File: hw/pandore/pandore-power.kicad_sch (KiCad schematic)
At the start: 57 parts, among them J14 V12, J20 V5, J21 V3.3, J32 VSTBY, J6 VIN, Q5 MOSFET_EN-N, Q6 MOSFET_EN-N, U19 AP6335xQ, U20 AP6335xQ, U27 LDL212DR

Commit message: added monitor amp with volume knob continue routing all around
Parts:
- R129, R133: now not fitted
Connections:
- net PWRON: now also R129.2, R130.1, R133.2, R134.1, U19.2 (EN), U20.2 (EN)
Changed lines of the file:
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@@
 	)
 	(junction
+		(at 97.79 116.84)
+		(diameter 0)
+		(color 0 0 0 0)
+	)
+	(junction
 		(at 101.6 35.56)
 		(diameter 0)
@@
 	(wire
 		(pts
+			(xy 97.79 116.84) (xy 97.79 68.58)
+		)
+		(stroke
+			(width 0)
+			(type default)
+		)
+	)
+	(wire
+		(pts
 			(xy 92.71 35.56) (xy 92.71 38.1)
 		)
@@
 	(wire
 		(pts
-			(xy 33.02 116.84) (xy 48.26 116.84)
+			(xy 33.02 116.84) (xy 97.79 116.84)
 		)
 		(stroke
@@
 	(wire
 		(pts
+			(xy 97.79 68.58) (xy 123.19 68.58)
+		)
+		(stroke
+			(width 0)
+			(type default)
+		)
+	)
+	(wire
+		(pts
 			(xy 182.88 55.88) (xy 182.88 57.15)
 		)
@@
 	(wire
 		(pts
+			(xy 97.79 116.84) (xy 123.19 116.84)
+		)
+		(stroke
+			(width 0)
+			(type default)
+		)
+	)
+	(wire
+		(pts
 			(xy 101.6 55.88) (xy 101.6 104.14)
 		)
@@
 		(in_bom yes)
 		(on_board yes)
-		(dnp no)
+		(dnp yes)
 		(fields_autoplaced yes)
 		(property "Reference" "R129"
@@
 		(in_bom yes)
 		(on_board yes)
-		(dnp no)
+		(dnp yes)
 		(fields_autoplaced yes)
 		(property "Reference" "R133"

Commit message: last sprint almost done, most routing done
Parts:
- added Q16: MOSFET_EN-P, reekilib_dfn:DFN65P300X300X100-9, symbol reekilib_mfe:MOSFET_EN-P_8pin
- added R276, R277: ${Resistance}, ${Tolerance}, ${Power}, reekilib_res:RESC1005, symbol reekilib_res:res
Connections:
- net V12: now also Q16.1 (S), Q16.2 (S), Q16.3 (S), R276.2
- net VSS: now also R277.1
- net at J6.1 (TIP): now also Q16.5 (D), Q16.6 (D), Q16.7 (D), Q16.8 (D), Q16.9 (D)
- new net: Q16.4 (G), R276.1, R277.2

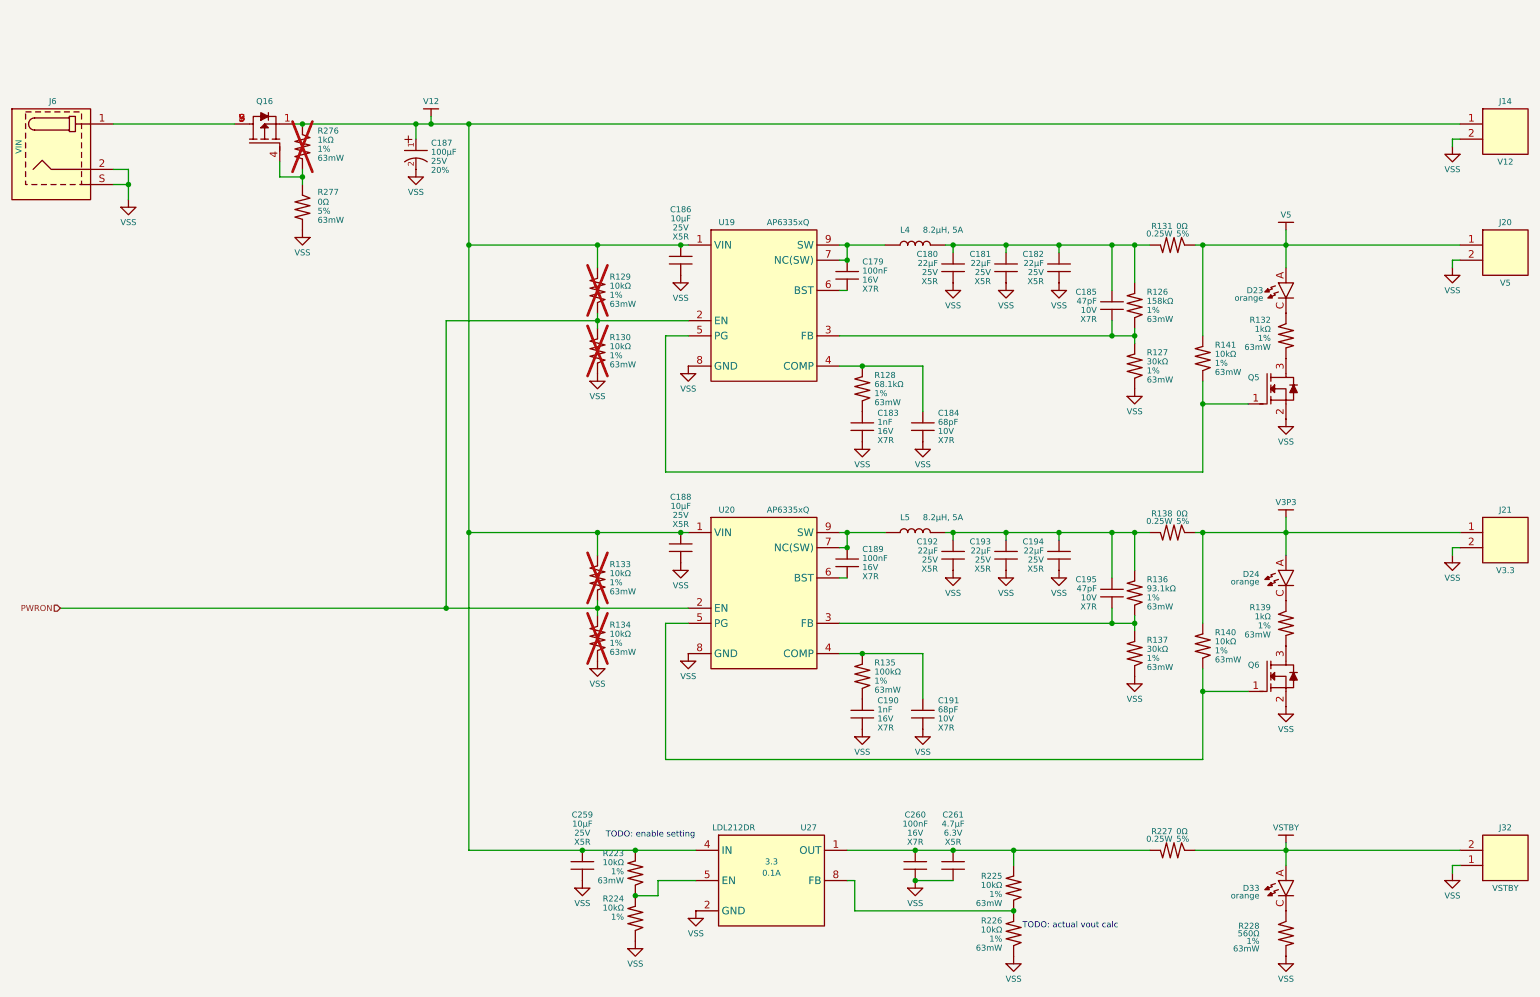
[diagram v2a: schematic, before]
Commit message: finished adding mpn,mfg to all parts, finished routing placement
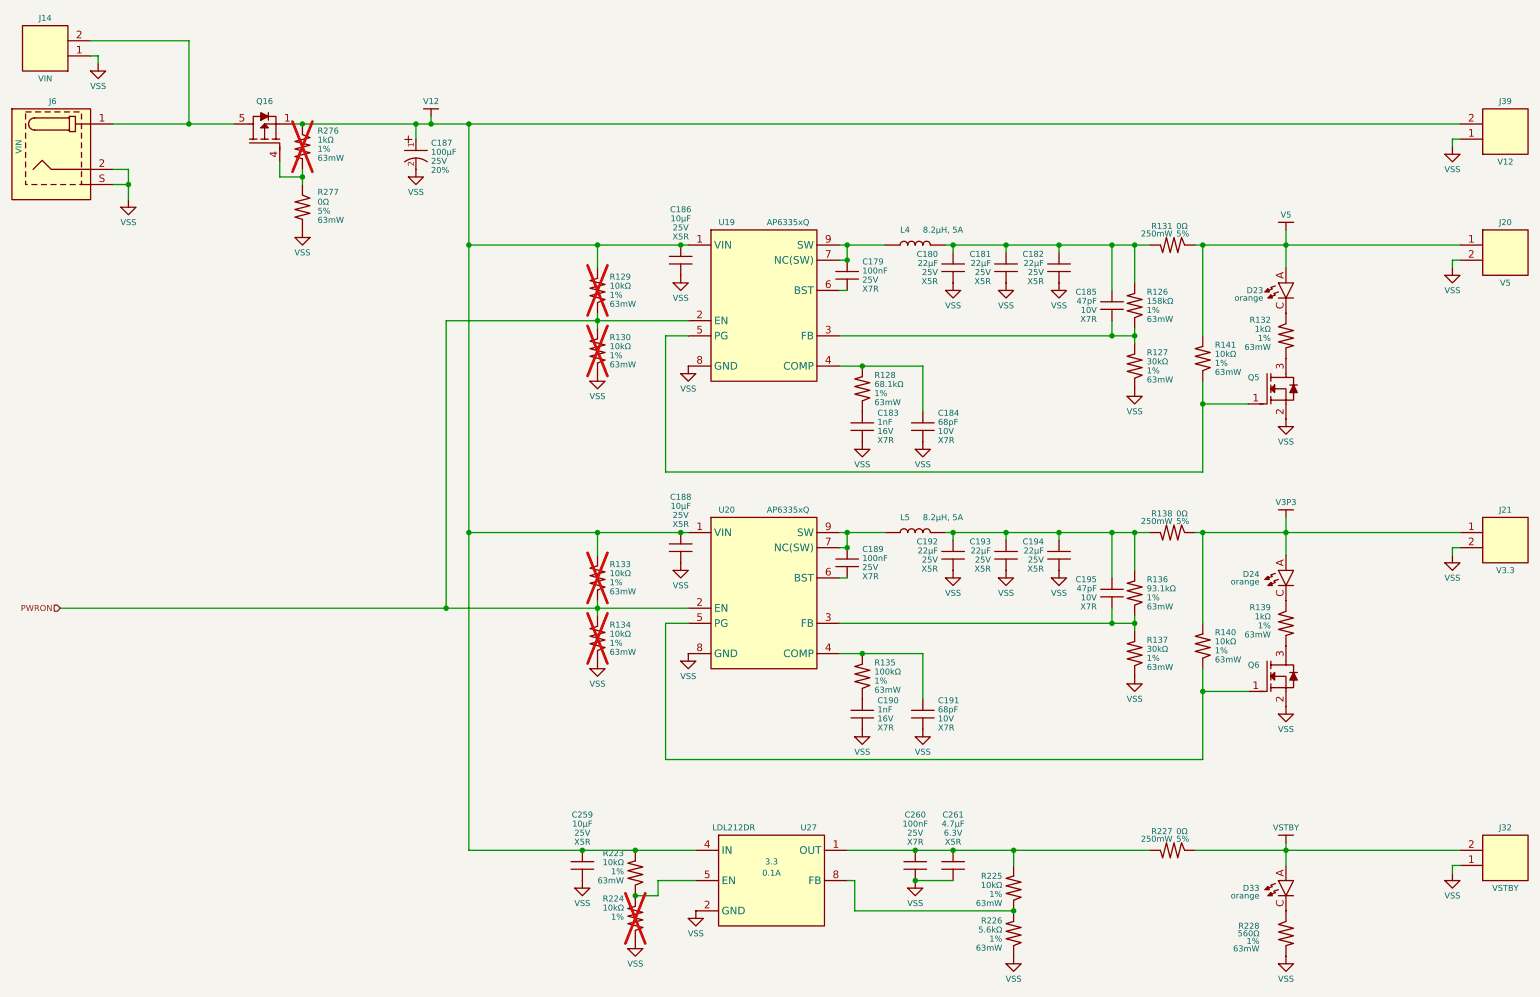
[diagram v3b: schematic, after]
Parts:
- added J39: V12, reekilib_con:HDR254P1X02-TH, symbol reekilib_con:hdr-1x2
- C179, C189, C260: MFG2 Samsung Electro-Mechanics -> (none); MFG3 Taiyo Yuden -> (none); MPN2 CL05B104KA5NNNC -> (none); MPN3 EMK105B7104KV-F -> (none); Voltage 16V -> 25V
- C183, C190: Link (none) -> https://yageogroup.com/products/Capacitors/part/CC0402KRX7R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; MFG (none) -> Yageo; MPN (none) -> CC0402KRX7R9BB102
- C184, C191: Link (none) -> https://yageogroup.com/products/Capacitors/part/CC0402JRNPO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; MFG (none) -> Yageo; MPN (none) -> CC0402JRNPO9BN680
- C185, C195: Link (none) -> https://yageogroup.com/products/Capacitors/part/CC0402JRNPO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; MFG (none) -> Yageo; MPN (none) -> CC0402JRNPO9BN470
- C186, C188, C259: MFG (none) -> Murata; MPN (none) -> GRM21BR61E106KA73K
- J14: value V12 -> VIN
- J32: MFG (none) -> Adam Tech; MPN (none) -> PH1-02-UA
- R126: Link (none) -> https://yageogroup.com/products/Resistors/part/RC0402FR-071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; MFG (none) -> YAGEO; MPN (none) -> RC0402FR-07158KL
- R127, R137: Link (none) -> https://yageogroup.com/products/Resistors/part/RC0402FR-073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; MFG (none) -> YAGEO; MPN (none) -> RC0402FR-0730KL
- R128: Link (none) -> https://yageogroup.com/products/Resistors/part/RC0402FR-076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; MFG (none) -> YAGEO; MPN (none) -> RC0402FR-0768K1L
- R131, R138, R227: Link (none) -> https://yageogroup.com/products/Resistors/part/RT0805DRE074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; MFG (none) -> YAGEO; MPN (none) -> RC0805JR-070RL; Power 0.25W -> 250mW
- R132, R139, R276: Link (none) -> https://yageogroup.com/products/Resistors/part/RC0402FR-131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; MFG (none) -> YAGEO; MPN (none) -> RC0402FR-131KL
- R135: Link (none) -> https://yageogroup.com/products/Resistors/part/RC0402FR-079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; MFG (none) -> YAGEO; MPN (none) -> RC0402FR-07100KL
- R136: Link (none) -> https://yageogroup.com/products/Resistors/part/RC0402FR-079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; MFG (none) -> YAGEO; MPN (none) -> RC0402FR-0793K1L
- R224: now not fitted
- R226: Link https://www.bourns.com/search?indexCatalogue=psindex&search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 -> https://yageogroup.com/products/Resistors/part/RC0402FR-075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; MFG Bourns Inc -> YAGEO; MFG2 Walsin Technology Corporation -> (none); MFG3 Yageo -> (none); MPN CR0402-FX-1002GLF -> RC0402FR-075K6L; MPN2 WR04X1002FTL -> (none); MPN3 RC0402FR-0710KL -> (none); Resistance 10kΩ -> 5.6kΩ
- R228: Link (none) -> https://yageogroup.com/products/Resistors/part/RC0402FR-075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; MFG (none) -> YAGEO; MPN (none) -> RC0402FR-07560RL
- R277: Link (none) -> https://yageogroup.com/products/Resistors/part/RC0402JR-070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; MFG (none) -> Yageo; MFG2 (none) -> Stackpole; MFG3 (none) -> Vishay Dale; MPN (none) -> RC0402JR-070RL; MPN2 (none) -> RMCF0402ZT0R00; MPN3 (none) -> CRCW04020000Z0ED
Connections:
- net V12: now also J39.2; no longer J14.1
- net VSS: now also J14.1, J39.1; no longer J14.2
- net at J6.1 (TIP), Q16.5 (D), Q16.6 (D)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: now also J14.2
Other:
- note removed: "TODO: actual vout calc"
- note removed: "TODO: enable setting"
- moved on the sheet: J14
